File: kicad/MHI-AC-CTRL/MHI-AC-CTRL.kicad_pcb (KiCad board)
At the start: 2 copper layers, 41.9 x 27.2 mm, 9 parts, among them J1 Conn_01x05, J3 Conn_01x03, U1 TSR_1-2450, U2 WeMos_D1_mini, U3 LEVEL-SHIFTER-4CH

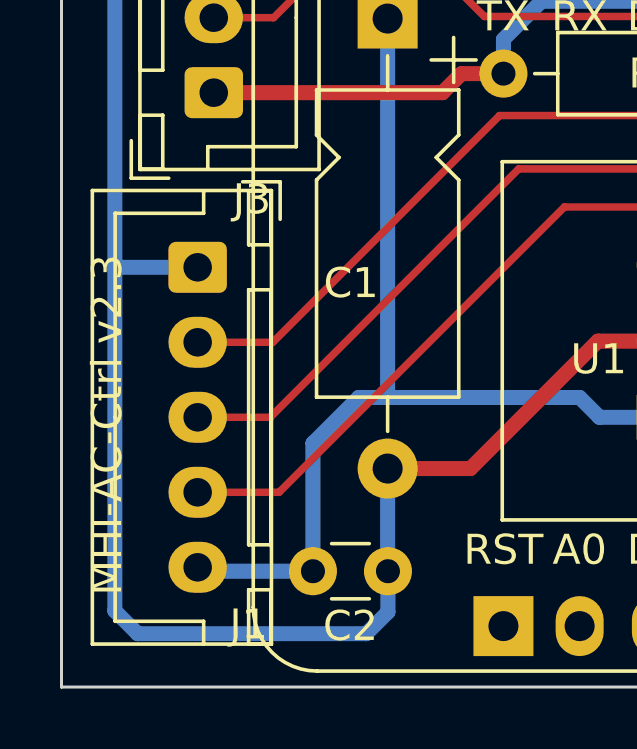
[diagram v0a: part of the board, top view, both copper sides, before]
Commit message: KiCad: Fix J1 connector (#155)
This fixes the J1 connector footprint and 3D model by using
easyeda2kicad [0] to pull the data from LCSC!

Closes #111

[0]: https://github.com/uPesy/easyeda2kicad.py

Signed-off-by: Olliver Schinagl <oliver@schinagl.nl>
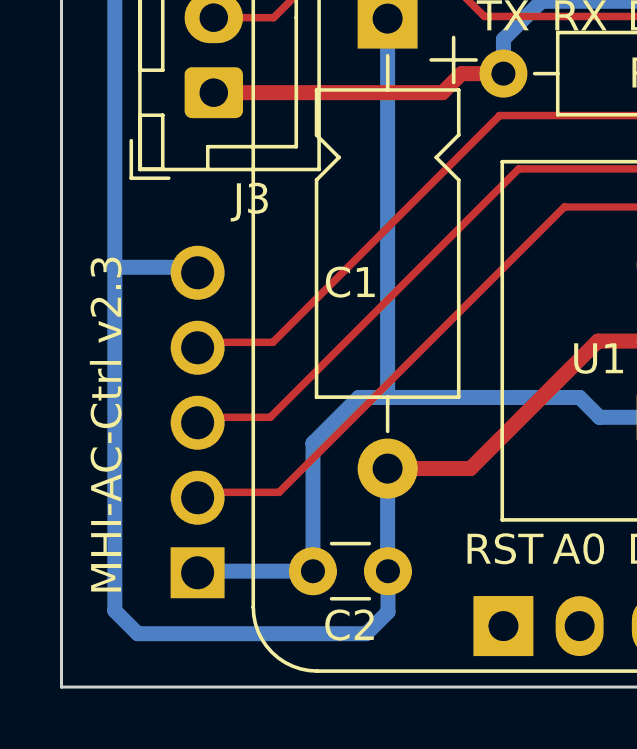
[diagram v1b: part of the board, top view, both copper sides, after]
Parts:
- J1: footprint Connector_JST:JST_XH_B5B-XH-A_1x05_P2.50mm_Vertical -> easyeda2kicad:CONN-TH_5P-P2.50_05JQ-BT; moved to B.Cu
- moved J1 5.18 mm to (83.8, 55.5)

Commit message: Correct J1 connector pinout (#168)
Fixes #167
Regenerated PDF and gerber/drill
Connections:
- J1 pad 1: GND -> +12V
- J1 pad 2: MISO_5V -> CLK_5V
- J1 pad 4: CLK_5V -> MISO_5V
- J1 pad 5: +12V -> GND
